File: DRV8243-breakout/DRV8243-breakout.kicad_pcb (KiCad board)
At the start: 2 copper layers, 50 x 40 mm, 27 parts, among them J1 Vin, J2 Motor_Output, J3 Conn_01x11_Pin, J4 Motor_Output, Q1 PMOS-AOD409, U1 PDRV8243HRXYQ1, U2 PDRV8243HRXYQ1

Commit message: Routing v2
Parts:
- J3: value Conn_01x11_Pin -> Conn_02x06_Odd_Even; footprint Connector_PinHeader_2.54mm:PinHeader_1x11_P2.54mm_Vertical -> Connector_PinSocket_2.54mm:PinSocket_2x06_P2.54mm_Vertical
- moved H1 65.6 mm to (219.0, 98.5)
- moved R3 40.4 mm to (195.8, 99.7), turned to 180 degrees
- moved R4 40.3 mm to (195.8, 105.8), turned to 180 degrees
- moved R5 40.0 mm to (195.8, 101.8), turned to 180 degrees
- moved R6 39.9 mm to (195.8, 103.8), turned to 180 degrees
- moved C4 25.3 mm to (166.8, 104.8), turned to 90 degrees
- moved R10 25.1 mm to (169.0, 104.9), turned to 90 degrees
- moved J3 21.9 mm to (185.2, 108.5), turned to -90 degrees
- moved H2 21.4 mm to (217.5, 113.5)
- moved R2 14.2 mm to (169.0, 109.3)
- moved C3 14.0 mm to (166.8, 109.3)
- moved R7 12.9 mm to (188.6, 108.9), turned to -90 degrees
- moved J1 9.00 mm to (168.0, 75.0)
- moved R1 5.00 mm to (160.9, 97.5), turned to 180 degrees
- moved C5 4.93 mm to (190.0, 95.6), turned to 90 degrees
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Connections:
- J3 pad 10: IPROPI1 -> IN3
- J3 pad 11: nFault -> IPROPI0
- J3 pad 2: Vcc -> nSLEEP
- J3 pad 3: nSLEEP -> Vcc
- J3 pad 5: IN1 -> nFault0
- J3 pad 6: IN2 -> nFault1
- J3 pad 7: IN3 -> IN2
- J3 pad 9: IPROPI0 -> IN1
- R7 pad 2: nFault -> nFault0
- R9 pad 2: nFault -> nFault1
- U1 pad 1: nFault -> nFault0
- U2 pad 1: nFault -> nFault1
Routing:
- net GND: track 0.00 -> 32.6 mm, vias 0 -> 12
- net VM: track 35.5 -> 59.2 mm
- net nFault0: track 0.00 -> 22.9 mm, vias 0 -> 1
- net nFault1: track 0.00 -> 19.6 mm, vias 0 -> 2
- net DIAG: track 16.9 -> 30.6 mm, vias 0 -> 2
- net IPROPI1: track 17.9 -> 5.77 mm
- net SR: track 17.5 -> 28.8 mm, vias 0 -> 2
- net Vcc: track 0.00 -> 8.46 mm
- net ITRIP: track 18.1 -> 26.3 mm, vias 0 -> 2
- net IN3: track 20.4 -> 13.3 mm, vias 2 -> 0
- net nFault: track 6.85 -> 0.00 mm
- net OUT4: track 32.4 -> 25.8 mm
- net OUT2: track 32.2 -> 25.8 mm
- net IPROPI0: track 12.1 -> 5.74 mm
- net MODE: track 18.8 -> 24.6 mm, vias 0 -> 2
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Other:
- board size 50 x 40 mm -> 42.5 x 42.5 mm

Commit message: Routing Etc
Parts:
- moved H1 58.4 mm to (161.5, 108.5)
- moved C2 7.22 mm to (170.6, 97.6), turned to -90 degrees
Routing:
- net IPROPI1: track 5.77 -> 38.0 mm, vias 0 -> 1
- net DRVOFF: track 0.00 -> 23.0 mm, vias 0 -> 3
- net IPROPI0: track 5.74 -> 20.6 mm, vias 0 -> 1
- net nSLEEP: track 12.7 -> 21.5 mm, vias 2 -> 3
- net nFault0: track 22.9 -> 25.1 mm, vias 1 -> 2
- net nFault1: track 19.6 -> 21.0 mm
- added copper zone on F.Cu, net GND

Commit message: Some Layout Refinement
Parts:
- moved H2 22.1 mm to (196.0, 108.5)
- moved R3 2.00 mm to (195.8, 97.7)
- moved R4 2.00 mm to (195.8, 103.8)
- moved R5 2.00 mm to (195.8, 99.8)
- moved R6 2.00 mm to (195.8, 101.8)
- moved C5 1.00 mm to (191.0, 95.6)
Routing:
- net VM: track 59.5 -> 34.2 mm
- net MODE: track 24.6 -> 25.4 mm
- net DIAG: track 30.6 -> 29.9 mm
- net nSLEEP: track 21.5 -> 22.1 mm
- added copper zone on F.Cu, net VM

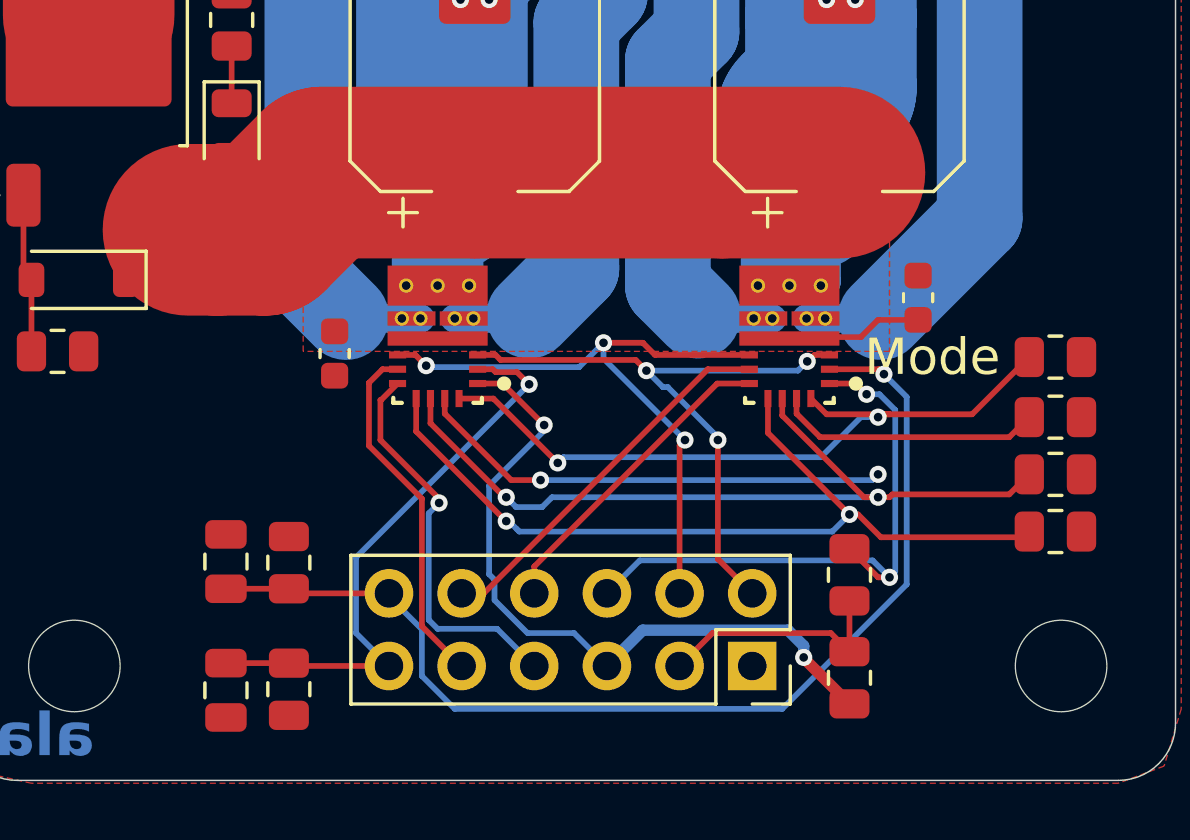
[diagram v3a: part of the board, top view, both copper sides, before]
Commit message: Update Silkscreen
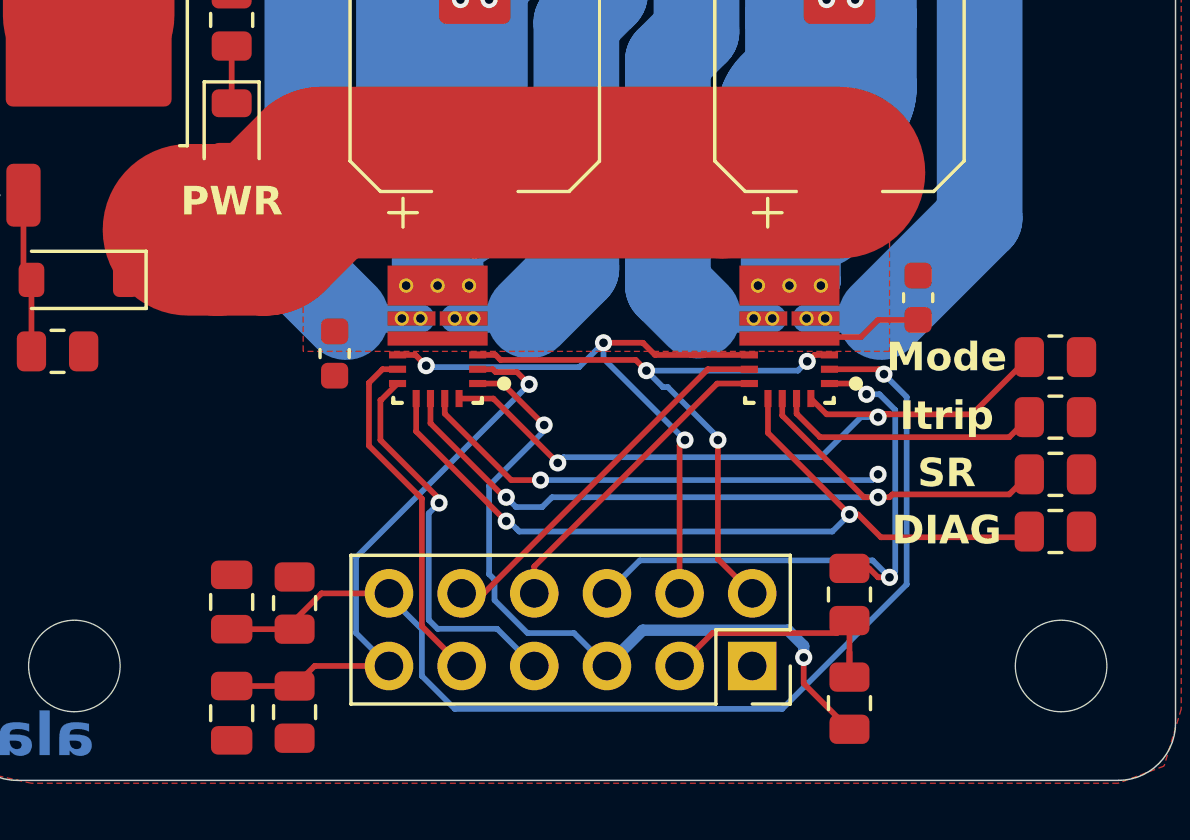
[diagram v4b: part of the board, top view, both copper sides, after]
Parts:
- moved C4 1.43 mm to (167.0, 106.3)
- moved R10 1.43 mm to (169.2, 106.3)
- moved R7 0.89 mm to (188.6, 109.8)
- moved C3 0.82 mm to (167.0, 110.2)
- moved R2 0.82 mm to (169.2, 110.1)
- moved R9 0.69 mm to (188.6, 106.0)
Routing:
- net Vcc: track 8.46 -> 9.46 mm
- net nFault0: track 25.1 -> 26.0 mm
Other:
- board text added: "DIAG"
- board text added: "DRV8243 J.YANN 2025"
- board text added: "Itrip"
- board text added: "PWR"
- board text added: "SR"
